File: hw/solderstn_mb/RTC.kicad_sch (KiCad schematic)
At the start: 12 parts, among them Q2101 AO3401A, Q2102 DMG1013T, U2101 DS3231M, U2102 AT24C256C-SSHL-T, U2103 DS3231MZ

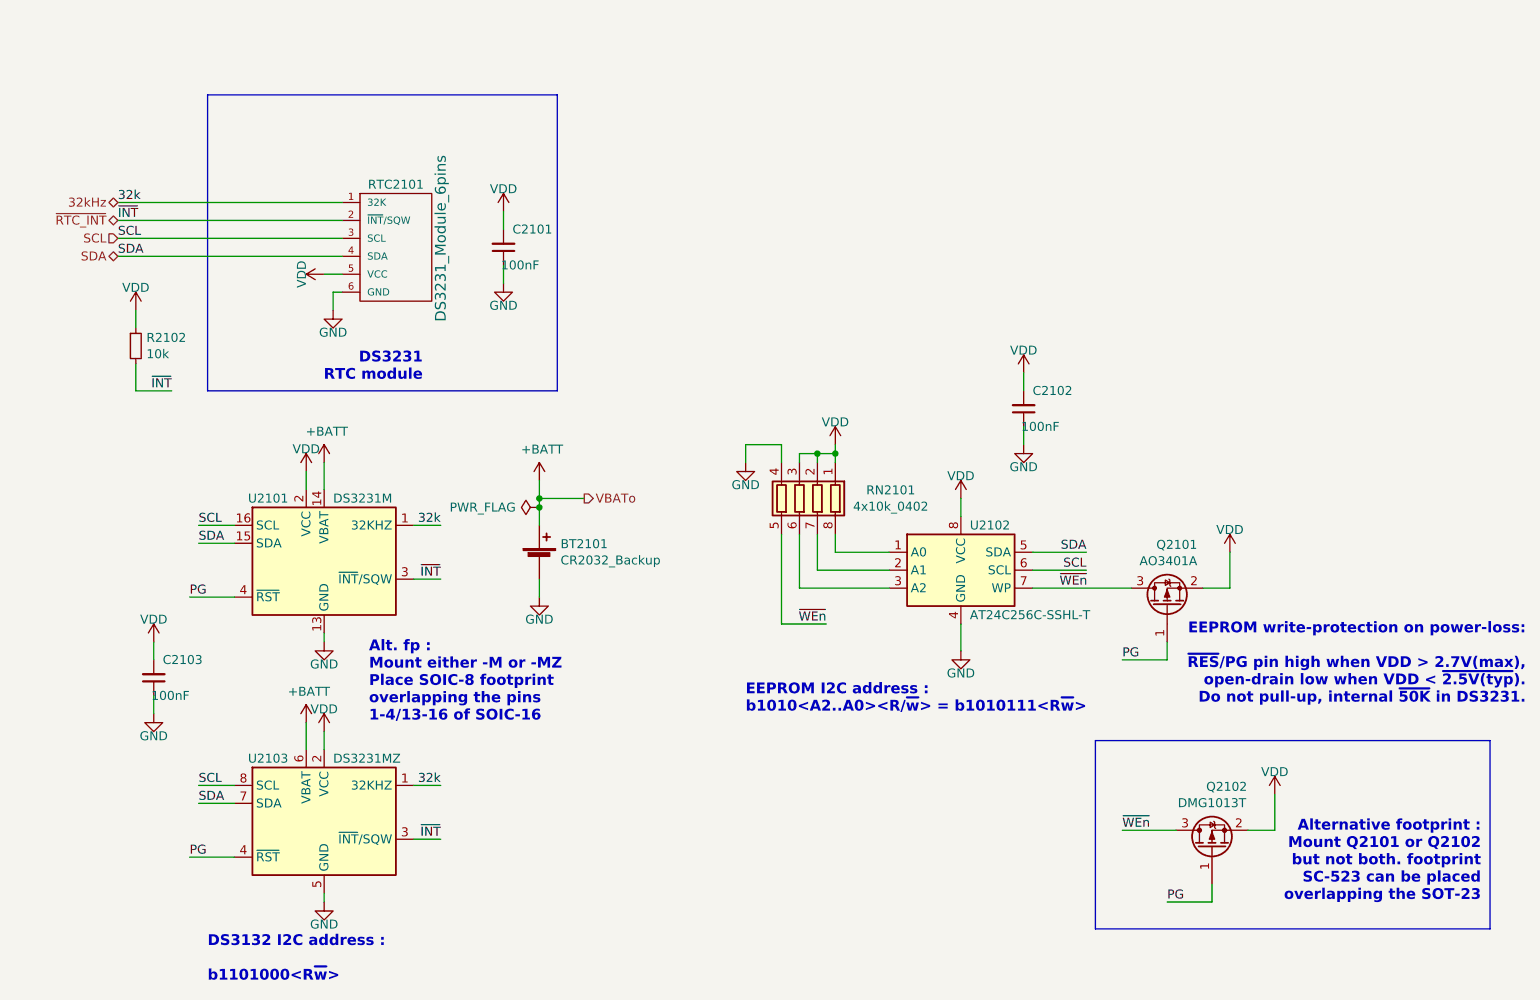
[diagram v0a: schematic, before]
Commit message: Placeholder 3d-models for rear-panel (w. conns), PSU, Bottom-plate, front-panel (w. conns), outer fp
With these placeholder mech. objects, the build-in 3d view of MB pcb features most of the mechanical
objects that constrain components placements. So 3d-view can be used to quickly check and iterate
placements to avoid 3d collisions, without having to first export MB STEP into FreeCAD and muck around
only to have to repeat again for each iteration
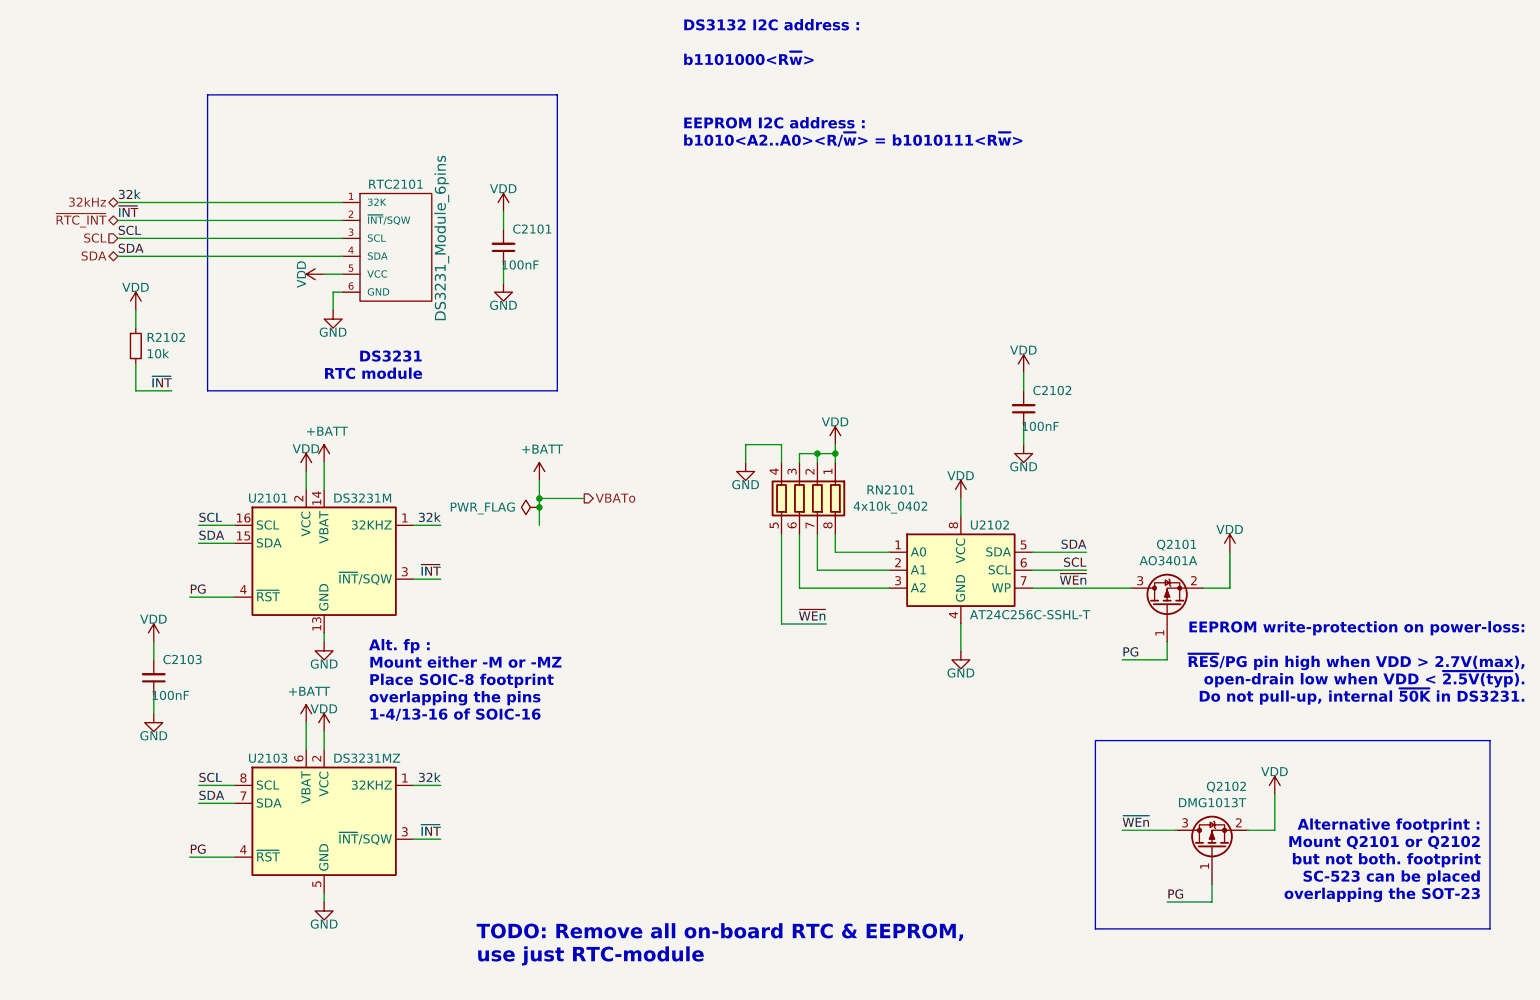
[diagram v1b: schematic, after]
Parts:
- removed BT2101: CR2032_Backup, customlib_mj_fp:CR2032_coincell_holder, symbol Device:Battery_Cell
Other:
- note added: "TODO: Remove all on-board RTC & EEPROM, use just RTC-module"
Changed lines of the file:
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@@
-    (stroke (width 0) (type default) (color 0 0 0 0))
-  )
-  (wire (pts (xy 105.41 105.41) (xy 105.41 102.87))
     (stroke (width 0) (type default) (color 0 0 0 0))
   )
@@
     (effects (font (size 1.524 1.524) (thickness 0.3048) bold) (justify left bottom))
   )
-  (text "DS3132 I2C address :\n\nb1101000<R~{w}>" (at 58.42 160.02 0)
+  (text "TODO: Remove all on-board RTC & EEPROM, \nuse just RTC-module"
+    (at 96.52 157.48 0)
+    (effects (font (size 2.032 2.032) (thickness 0.254) bold) (justify left bottom))
+  )
+  (text "DS3132 I2C address :\n\nb1101000<R~{w}>" (at 125.73 30.48 0)
     (effects (font (size 1.524 1.524) (thickness 0.3048) bold) (justify left bottom))
   )
@@
   )
   (text "EEPROM I2C address :\nb1010<A2..A0><R/~{w}> = b1010111<R~{w}>"
-    (at 134.62 121.92 0)
+    (at 125.73 41.91 0)
     (effects (font (size 1.524 1.524) (thickness 0.3048) bold) (justify left bottom))
   )
@@
     (effects (font (size 1.27 1.27)) (justify right))
   )
-  (symbol (lib_id "power:GND") (at 76.2 64.77 0)
+  (symbol (lib_id "power:GND") (at 76.2 64.77 0) (unit 1)
     (in_bom yes) (on_board yes)
     (property "Reference" "#PWR02104" (id 0) (at 76.2 71.12 0)
@@
     (pin "1")
   )
-  (symbol (lib_id "power:VDD") (at 74.93 59.69 90)
+  (symbol (lib_id "power:VDD") (at 74.93 59.69 90) (unit 1)
     (in_bom yes) (on_board yes)
     (property "Reference" "#PWR02102" (id 0) (at 78.74 59.69 0)
@@
     (pin "1")
   )
-  (symbol (lib_id "Device:C_Small") (at 100.33 55.88 180)
+  (symbol (lib_id "Device:C_Small") (at 100.33 55.88 180) (unit 1)
     (in_bom yes) (on_board yes)
     (property "Reference" "C2101" (id 0) (at 101.6 53.34 0)
@@
     (pin "2")
   )
-  (symbol (lib_id "power:VDD") (at 100.33 50.8 0)
+  (symbol (lib_id "power:VDD") (at 100.33 50.8 0) (unit 1)
     (in_bom yes) (on_board yes)
     (property "Reference" "#PWR02101" (id 0) (at 100.33 54.61 0)
@@
     (pin "1")
   )
-  (symbol (lib_id "customlib_mj:DS3231_Module_6pins") (at 85.09 54.61 0)
+  (symbol (lib_id "customlib_mj:DS3231_Module_6pins") (at 85.09 54.61 0) (unit 1)
     (in_bom yes) (on_board yes)
     (property "Reference" "RTC2101" (id 0) (at 85.09 46.99 0))
@@
     (pin "6")
   )
-  (symbol (lib_id "power:GND") (at 100.33 60.96 0)
+  (symbol (lib_id "power:GND") (at 100.33 60.96 0) (unit 1)
     (in_bom yes) (on_board yes)
     (property "Reference" "#PWR02103" (id 0) (at 100.33 67.31 0)
@@
     (pin "1")
   )
-  (symbol (lib_id "power:VDD") (at 72.39 87.63 0)
+  (symbol (lib_id "power:VDD") (at 72.39 87.63 0) (unit 1)
     (in_bom yes) (on_board yes)
     (property "Reference" "#PWR02109" (id 0) (at 72.39 91.44 0)
@@
     (pin "1")
   )
-  (symbol (lib_id "power:VDD") (at 74.93 124.46 0)
+  (symbol (lib_id "power:VDD") (at 74.93 124.46 0) (unit 1)
     (in_bom yes) (on_board yes)
     (property "Reference" "#PWR02120" (id 0) (at 74.93 128.27 0)
@@
     (pin "1")
   )
-  (symbol (lib_id "power:GND") (at 74.93 111.76 0)
+  (symbol (lib_id "power:GND") (at 74.93 111.76 0) (unit 1)
     (in_bom yes) (on_board yes)
     (property "Reference" "#PWR02115" (id 0) (at 74.93 118.11 0)
@@
     (pin "1")
   )
-  (symbol (lib_id "power:GND") (at 74.93 148.59 0)
+  (symbol (lib_id "power:GND") (at 74.93 148.59 0) (unit 1)
     (in_bom yes) (on_board yes)
     (property "Reference" "#PWR02122" (id 0) (at 74.93 154.94 0)
@@
     (pin "1")
   )
-  (symbol (lib_id "Device:C_Small") (at 50.8 116.84 180)
+  (symbol (lib_id "Device:C_Small") (at 50.8 116.84 180) (unit 1)
     (in_bom yes) (on_board yes)
     (property "Reference" "C2103" (id 0) (at 52.07 114.3 0)
@@
     (pin "2")
   )
-  (symbol (lib_id "Device:Battery_Cell") (at 105.41 100.33 0) (unit 1)
-    (in_bom yes) (on_board yes)
-    (property "Reference" "BT2101" (id 0) (at 108.4072 97.8916 0)
-      (effects (font (size 1.27 1.27)) (justify left))
-    )
-    (property "Value" "CR2032_Backup" (id 1) (at 108.4072 100.203 0)
-      (effects (font (size 1.27 1.27)) (justify left))
-    )
-    (property "Footprint" "customlib_mj_fp:CR2032_coincell_holder" (id 2) (at 105.41 98.806 90)
-      (effects (font (size 1.27 1.27)) hide)
-    )
-    (property "Datasheet" "https://lcsc.com/product-detail/Battery-Holders-Clips-Contacts_CR2032battery-Gold-plated-patch-horizontal-base_C70378.html" (id 3) (at 105.41 98.806 90)
-      (effects (font (size 1.27 1.27)) hide)
-    )
-    (pin "1")
-    (pin "2")
-  )
-  (symbol (lib_id "power:VDD") (at 50.8 111.76 0)
+  (symbol (lib_id "power:VDD") (at 50.8 111.76 0) (unit 1)
     (in_bom yes) (on_board yes)
     (property "Reference" "#PWR02114" (id 0) (at 50.8 115.57 0)
@@
     (pin "1")
   )
-  (symbol (lib_id "power:GND") (at 50.8 121.92 0)
+  (symbol (lib_id "power:GND") (at 50.8 121.92 0) (unit 1)
     (in_bom yes) (on_board yes)
     (property "Reference" "#PWR02118" (id 0) (at 50.8 128.27 0)
@@
     )
     (property "Datasheet" "" (id 3) (at 105.41 88.9 0)
-      (effects (font (size 1.27 1.27)) hide)
-    )
-    (pin "1")
-  )
-  (symbol (lib_id "power:GND") (at 105.41 105.41 0)
-    (in_bom yes) (on_board yes)
-    (property "Reference" "#PWR02113" (id 0) (at 105.41 111.76 0)
-      (effects (font (size 1.27 1.27)) hide)
-    )
-    (property "Value" "GND" (id 1) (at 105.41 108.585 0))
-    (property "Footprint" "" (id 2) (at 105.41 105.41 0)
-      (effects (font (size 1.27 1.27)) hide)
-    )
-    (property "Datasheet" "" (id 3) (at 105.41 105.41 0)
       (effects (font (size 1.27 1.27)) hide)
     )
@@
     (pin "8")
   )
-  (symbol (lib_id "power:GND") (at 165.1 113.03 0)
+  (symbol (lib_id "power:GND") (at 165.1 113.03 0) (unit 1)
     (in_bom yes) (on_board yes)
     (property "Reference" "#PWR02116" (id 0) (at 165.1 119.38 0)
@@
     (pin "1")
   )
-  (symbol (lib_id "power:VDD") (at 165.1 91.44 0)
+  (symbol (lib_id "power:VDD") (at 165.1 91.44 0) (unit 1)
     (in_bom yes) (on_board yes)
     (property "Reference" "#PWR02111" (id 0) (at 165.1 95.25 0)
@@
     (pin "1")
   )
-  (symbol (lib_id "Device:C_Small") (at 173.99 78.74 180)
+  (symbol (lib_id "Device:C_Small") (at 173.99 78.74 180) (unit 1)
     (in_bom yes) (on_board yes)
     (property "Reference" "C2102" (id 0) (at 175.26 76.2 0)
@@
     (pin "2")
   )
-  (symbol (lib_id "power:VDD") (at 173.99 73.66 0)
+  (symbol (lib_id "power:VDD") (at 173.99 73.66 0) (unit 1)
     (in_bom yes) (on_board yes)
     (property "Reference" "#PWR02105" (id 0) (at 173.99 77.47 0)
@@
     (pin "1")
   )
-  (symbol (lib_id "power:GND") (at 173.99 83.82 0)
+  (symbol (lib_id "power:GND") (at 173.99 83.82 0) (unit 1)
     (in_bom yes) (on_board yes)
     (property "Reference" "#PWR02107" (id 0) (at 173.99 90.17 0)
@@
     (pin "3")
   )
-  (symbol (lib_id "power:VDD") (at 203.2 99.06 0)
+  (symbol (lib_id "power:VDD") (at 203.2 99.06 0) (unit 1)
     (in_bom yes) (on_board yes)
     (property "Reference" "#PWR02112" (id 0) (at 203.2 102.87 0)
@@
     (pin "1")
   )
-  (symbol (lib_id "power:VDD") (at 147.32 83.82 0)
+  (symbol (lib_id "power:VDD") (at 147.32 83.82 0) (unit 1)
     (in_bom yes) (on_board yes)
     (property "Reference" "#PWR02106" (id 0) (at 147.32 87.63 0)
@@
     (pin "3")
   )
-  (symbol (lib_id "power:VDD") (at 209.55 133.35 0)
+  (symbol (lib_id "power:VDD") (at 209.55 133.35 0) (unit 1)
     (in_bom yes) (on_board yes)
     (property "Reference" "#PWR02121" (id 0) (at 209.55 137.16 0)
@@
     (pin "8")
   )
-  (symbol (lib_id "power:GND") (at 134.62 86.36 0)
+  (symbol (lib_id "power:GND") (at 134.62 86.36 0) (unit 1)
     (in_bom yes) (on_board yes)
     (property "Reference" "#PWR02123" (id 0) (at 134.62 92.71 0)
@@
     (pin "2")
   )
-  (symbol (lib_id "power:VDD") (at 48.26 64.77 0)
+  (symbol (lib_id "power:VDD") (at 48.26 64.77 0) (unit 1)
     (in_bom yes) (on_board yes)
     (property "Reference" "#PWR02124" (id 0) (at 48.26 68.58 0)

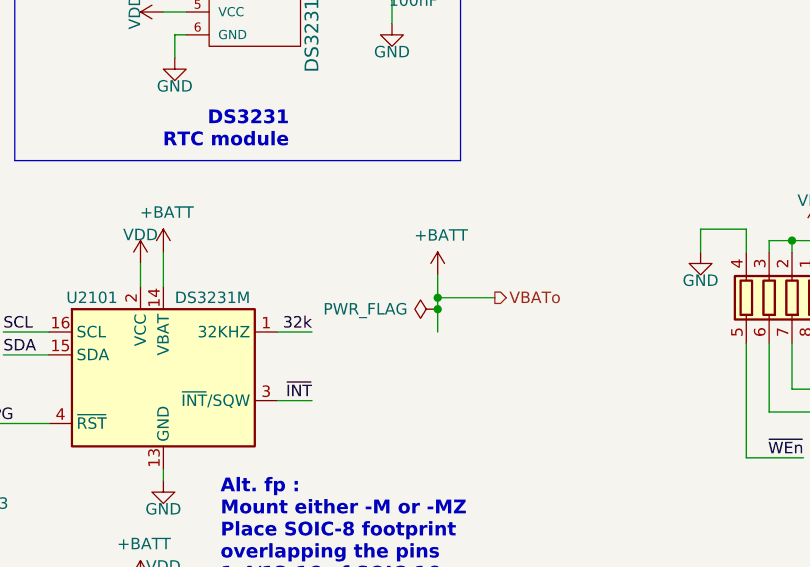
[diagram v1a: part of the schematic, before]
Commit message: hw: long-standing uncommitted stuff; mostly auto-updates (v7) fw: remove L052 tree (CMSIS & std-HAL shouldn't be committed and it was the wrong device name anyway)
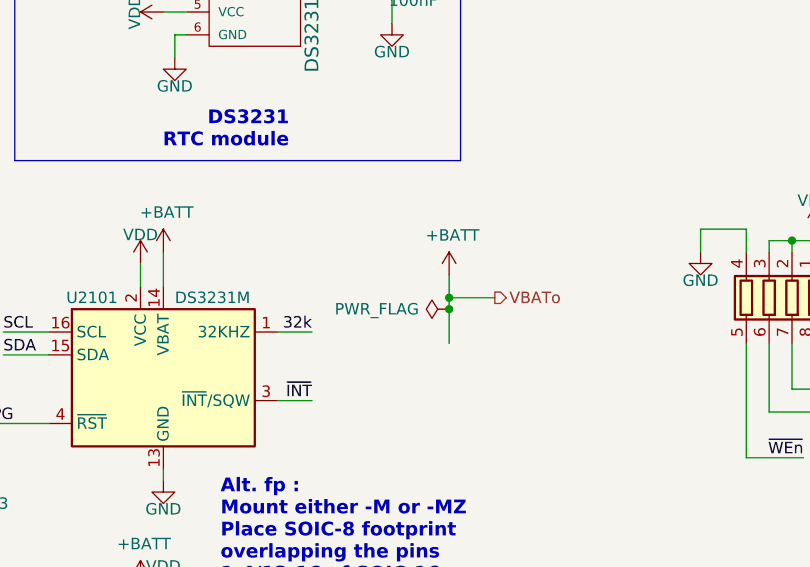
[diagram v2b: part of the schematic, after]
